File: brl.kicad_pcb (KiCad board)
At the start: 2 copper layers, 46 x 60 mm, 13 parts, among them J1 Screw_Terminal_01x04, J2 Screw_Terminal_01x04, Q1 Q_NMOS_GDS, U1 LM324A

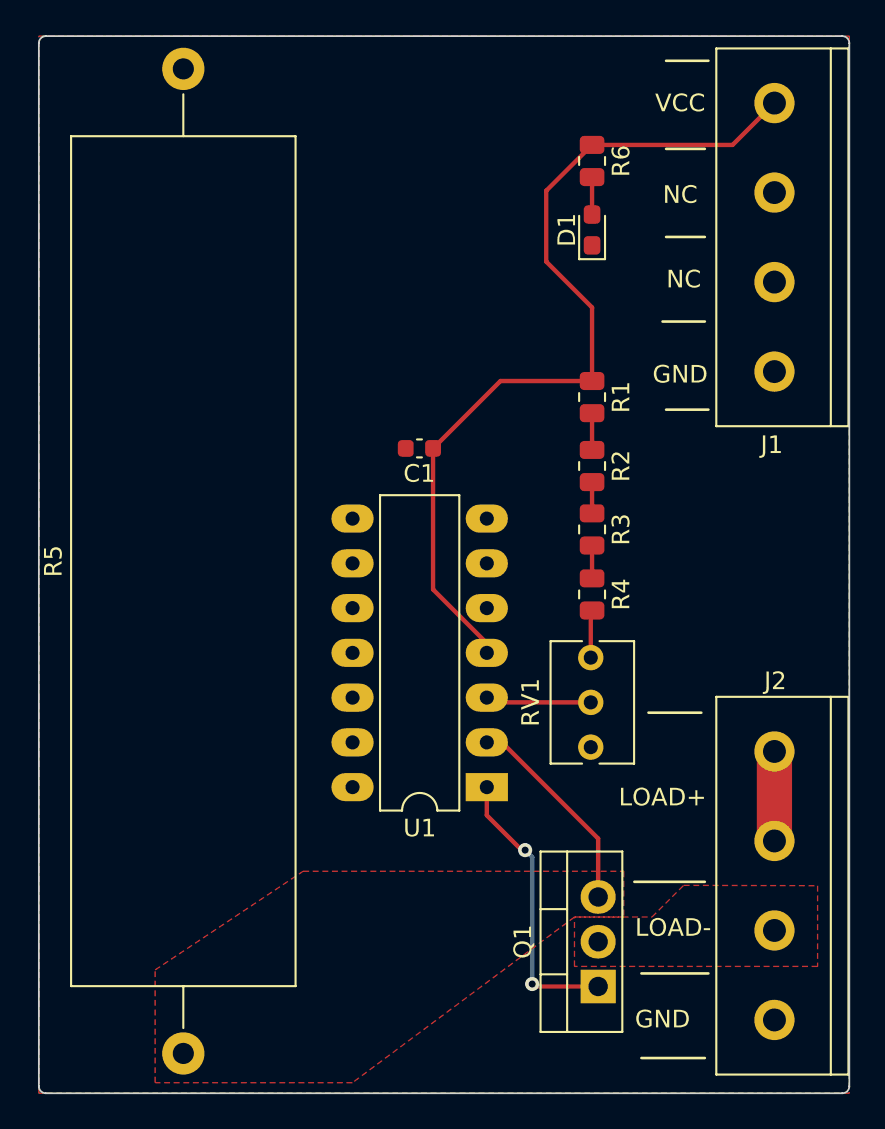
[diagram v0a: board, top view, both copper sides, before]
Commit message: added silkscreen bits
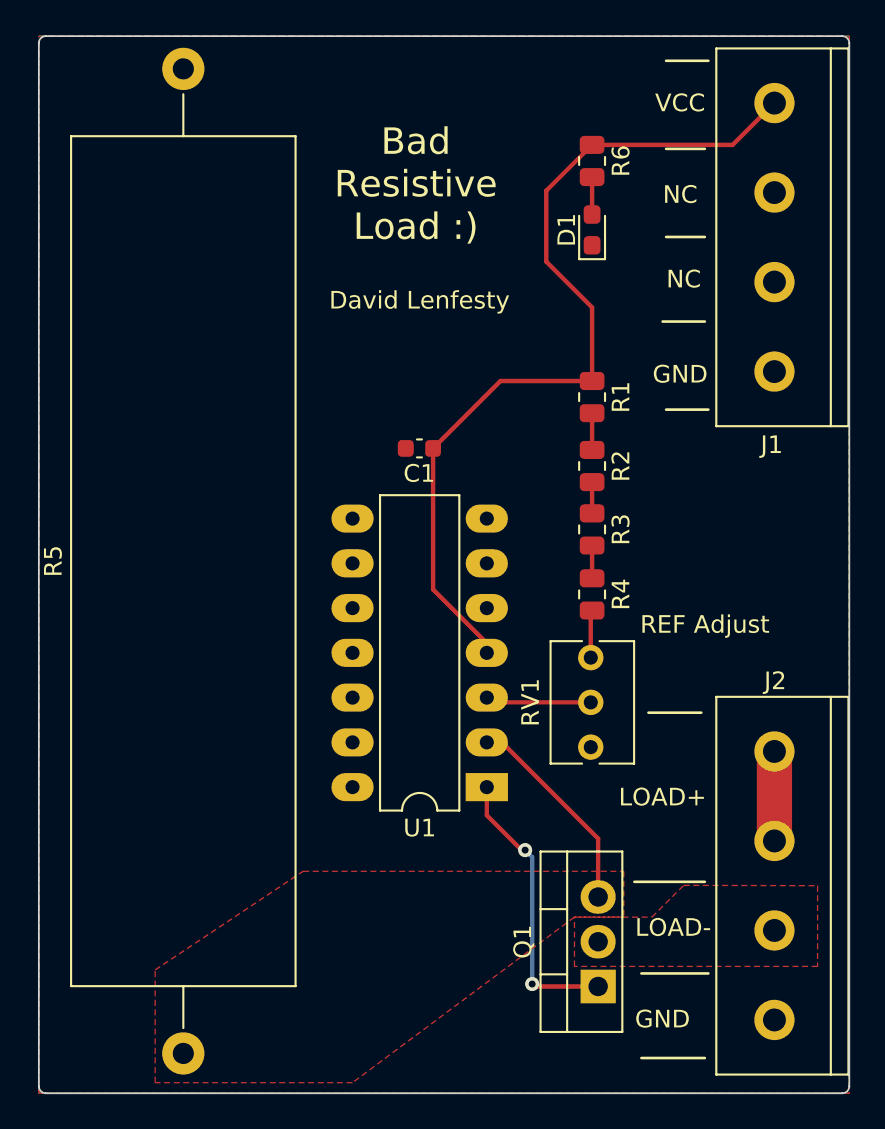
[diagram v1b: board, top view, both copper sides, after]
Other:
- board text added: "Bad Resistive Load :)"
- board text added: "David Lenfesty"
- board text added: "REF Adjust"
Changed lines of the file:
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@@
+    (effects (font (size 1 1) (thickness 0.15)))
+  )
+  (gr_text "David Lenfesty" (at 117.6 45) (layer "F.SilkS")
+    (effects (font (size 1 1) (thickness 0.15)))
+  )
+  (gr_text "REF Adjust" (at 133.8 63.4) (layer "F.SilkS")
     (effects (font (size 1 1) (thickness 0.15)))
   )
@@
     (effects (font (size 1 1) (thickness 0.15)))
   )
+  (gr_text "Bad\nResistive\nLoad :)" (at 117.4 38.4) (layer "F.SilkS")
+    (effects (font (size 1.5 1.5) (thickness 0.3)))
+  )
   (gr_text "VCC" (at 132.4 33.8) (layer "F.SilkS")
